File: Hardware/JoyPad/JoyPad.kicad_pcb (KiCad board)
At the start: 2 copper layers, 162.6 x 61 mm, 19 parts, among them J1 JOYPORT, SW1 DOWN, SW2 LEFT, SW3 RIGHT, SW4 A, SW5 B, SW6 SELECT, SW7 START, SW8 UP, U1 4021

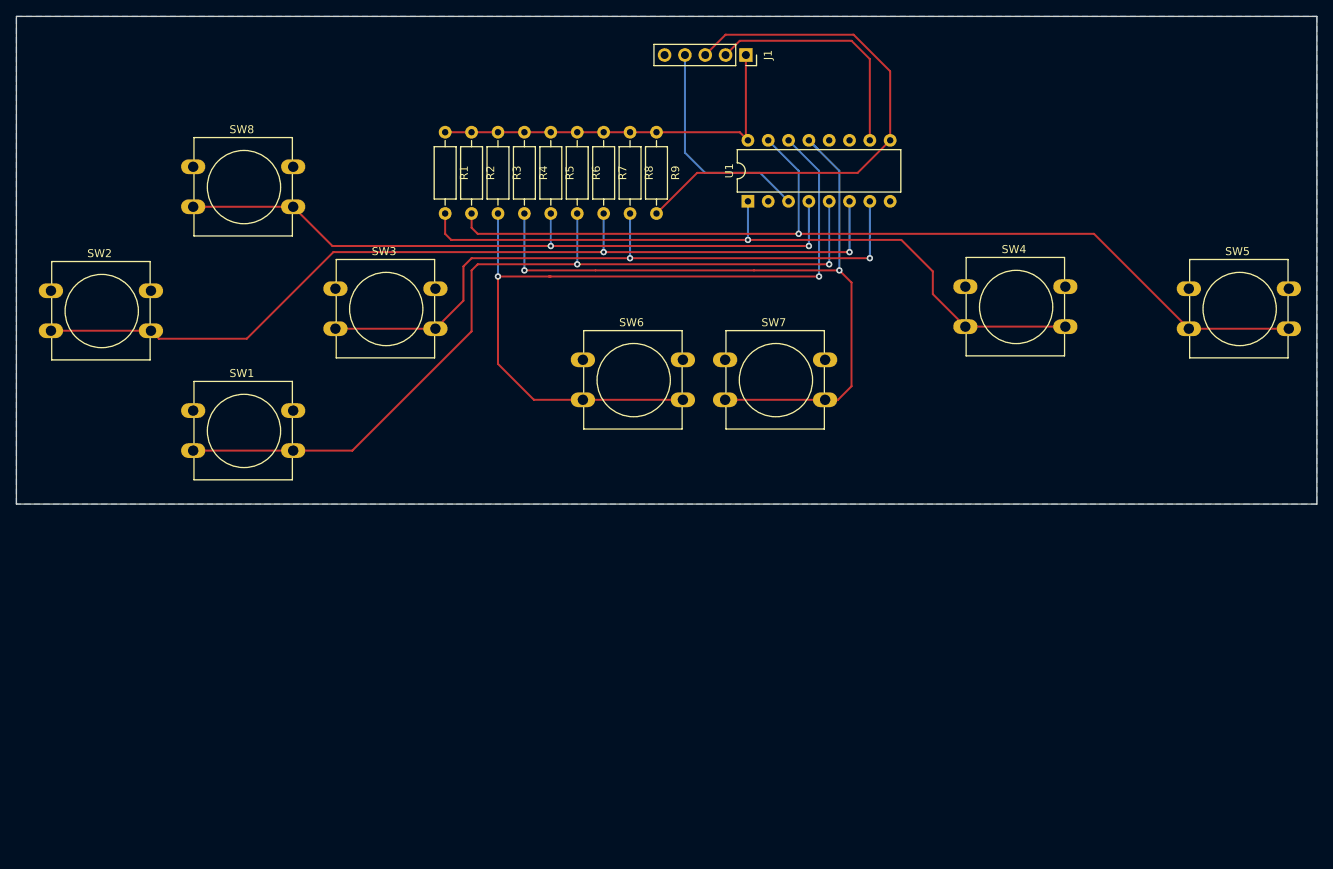
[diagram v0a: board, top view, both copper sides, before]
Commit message: Implement DMA and PCB ports
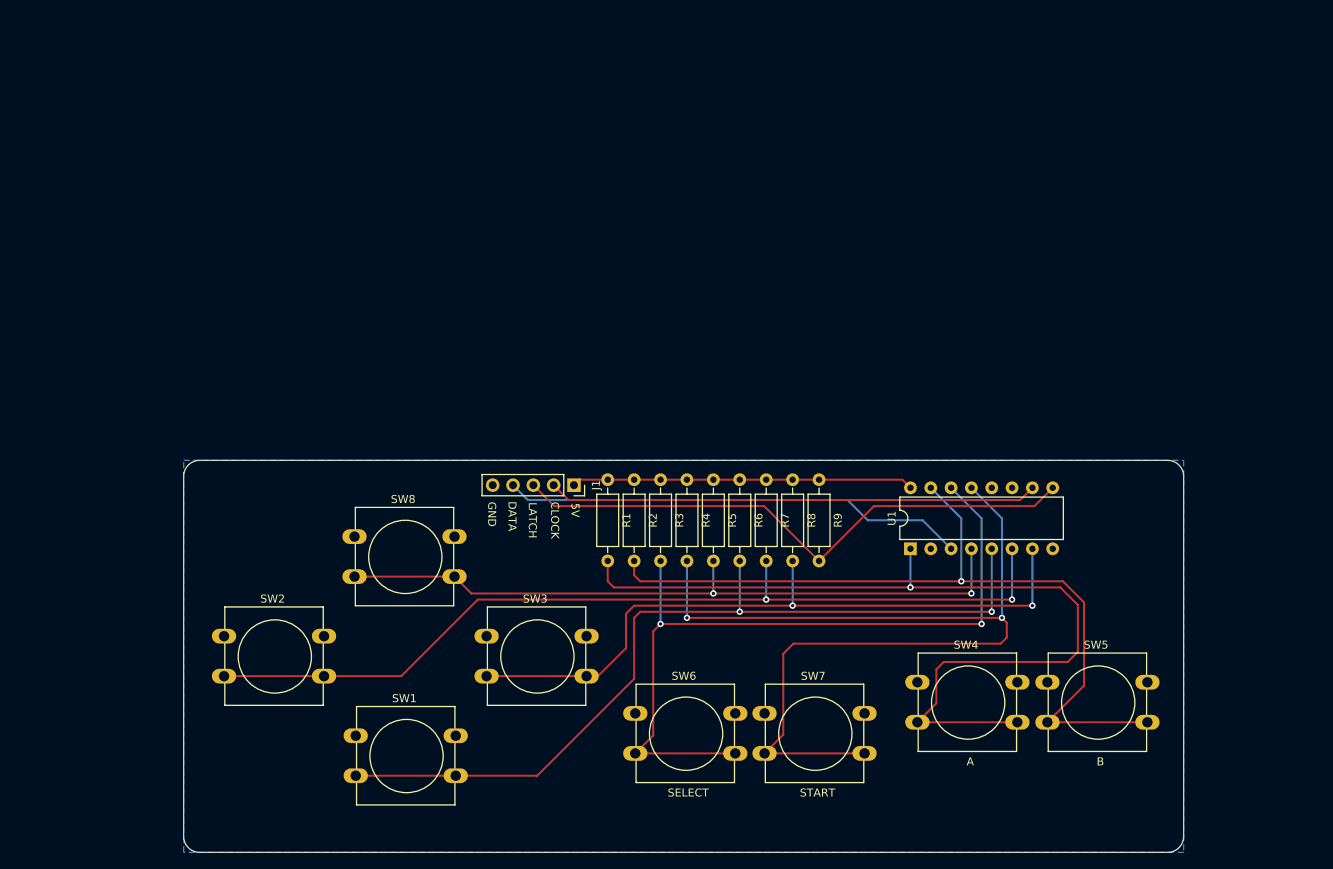
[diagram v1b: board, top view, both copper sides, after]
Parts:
- moved J1 57.9 mm to (118.0, 78.9)
- moved SW5 52.3 mm to (177.1, 103.6)
- moved SW8 50.4 mm to (90.5, 85.3)
- moved SW4 49.8 mm to (160.9, 103.6)
- moved SW2 48.3 mm to (74.2, 97.8)
- moved R1 48.0 mm to (122.2, 78.2)
- moved R4 48.0 mm to (132.1, 78.2)
- moved R5 48.0 mm to (135.4, 78.2)
- moved R8 48.0 mm to (145.3, 78.2)
- moved U1 48.0 mm to (160.0, 86.9)
- moved R2 48.0 mm to (125.5, 78.2)
- moved R3 48.0 mm to (128.8, 78.2)
- moved R6 48.0 mm to (138.7, 78.2)
- moved R7 48.0 mm to (142.0, 78.2)
- moved R9 48.0 mm to (148.6, 78.2)
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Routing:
- net CLOCK: track 29.9 -> 61.2 mm
- net OUTPUT: track 27.7 -> 58.1 mm
- net Net-(R4-Pad2): track 97.7 -> 121.7 mm
- net Net-(R1-Pad2): track 91.4 -> 111.9 mm
- net Net-(R2-Pad2): track 122.4 -> 102.1 mm
- net +5V: track 49.0 -> 41.8 mm
- net Net-(R3-Pad2): track 102.8 -> 96.6 mm
- net LATCH: track 67.7 -> 72.6 mm
- net Net-(R7-Pad2): track 115.9 -> 113.6 mm
- net Net-(R8-Pad2): track 85.7 -> 87.1 mm
- net Net-(R6-Pad2): track 107.8 -> 106.7 mm
- net Net-(R5-Pad2): track 88.6 -> 87.6 mm
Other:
- board size 162.6 x 61 mm -> 125 x 49 mm
- board text added: "5V"
- board text added: "CLOCK"
- board text added: "DATA"
- board text added: "GND"
- board text added: "LATCH"

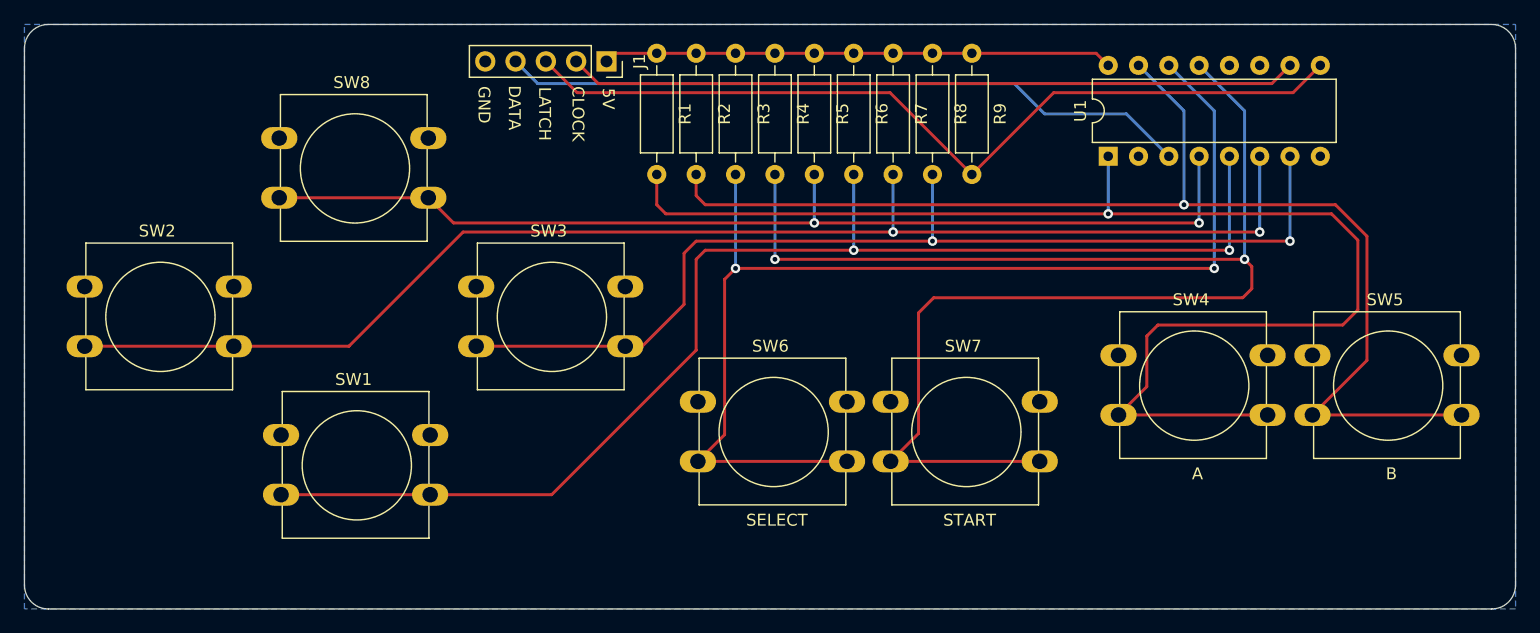
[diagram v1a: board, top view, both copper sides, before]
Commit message: Update to Kicad 6.0
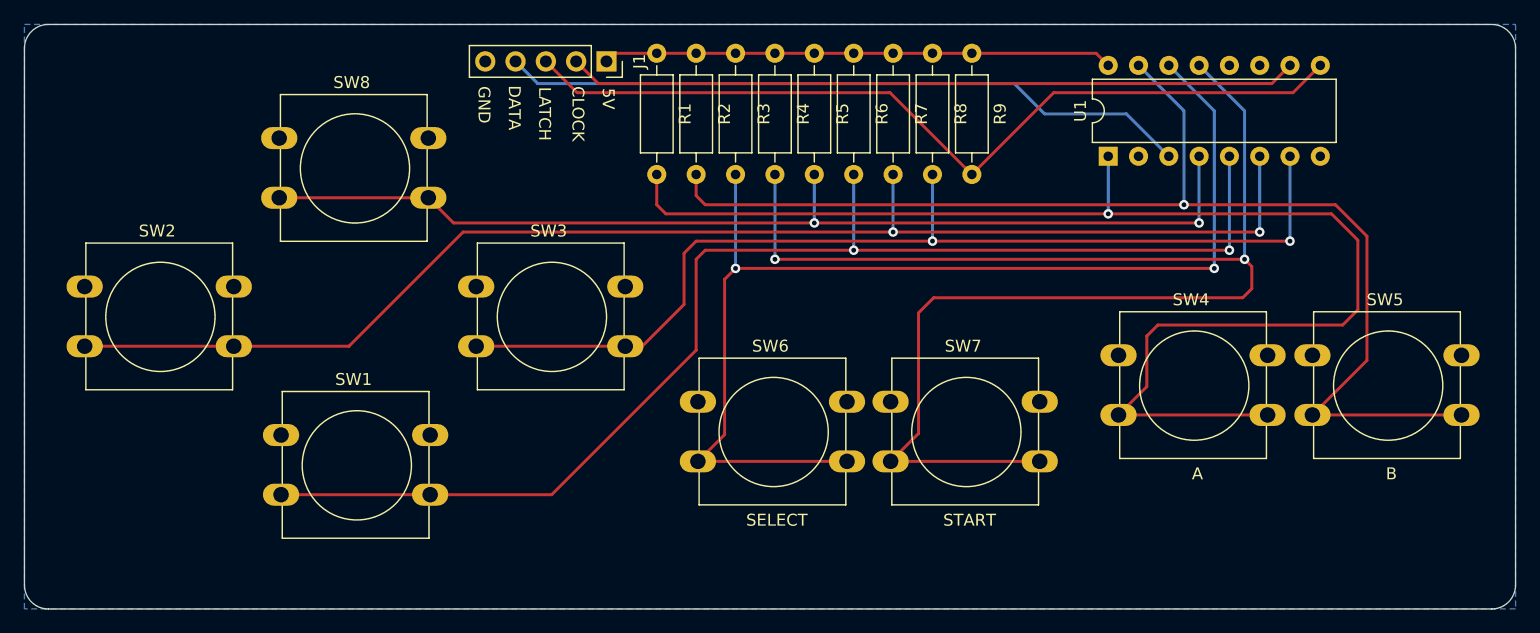
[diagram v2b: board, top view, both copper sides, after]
